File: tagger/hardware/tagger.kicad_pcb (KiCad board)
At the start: 4 copper layers, 70 x 40 mm, 77 parts, among them J1 XBEE_BOOTLOADER, J2 MICRO_SD_CARD, J4 SWD, J6 TETHER_POWER, J7 TETHER_DATA, J8 DISPLAY, J9 IO_CONN, SW1 COMMISSION, SW2 RESET, SW24 BOOT0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

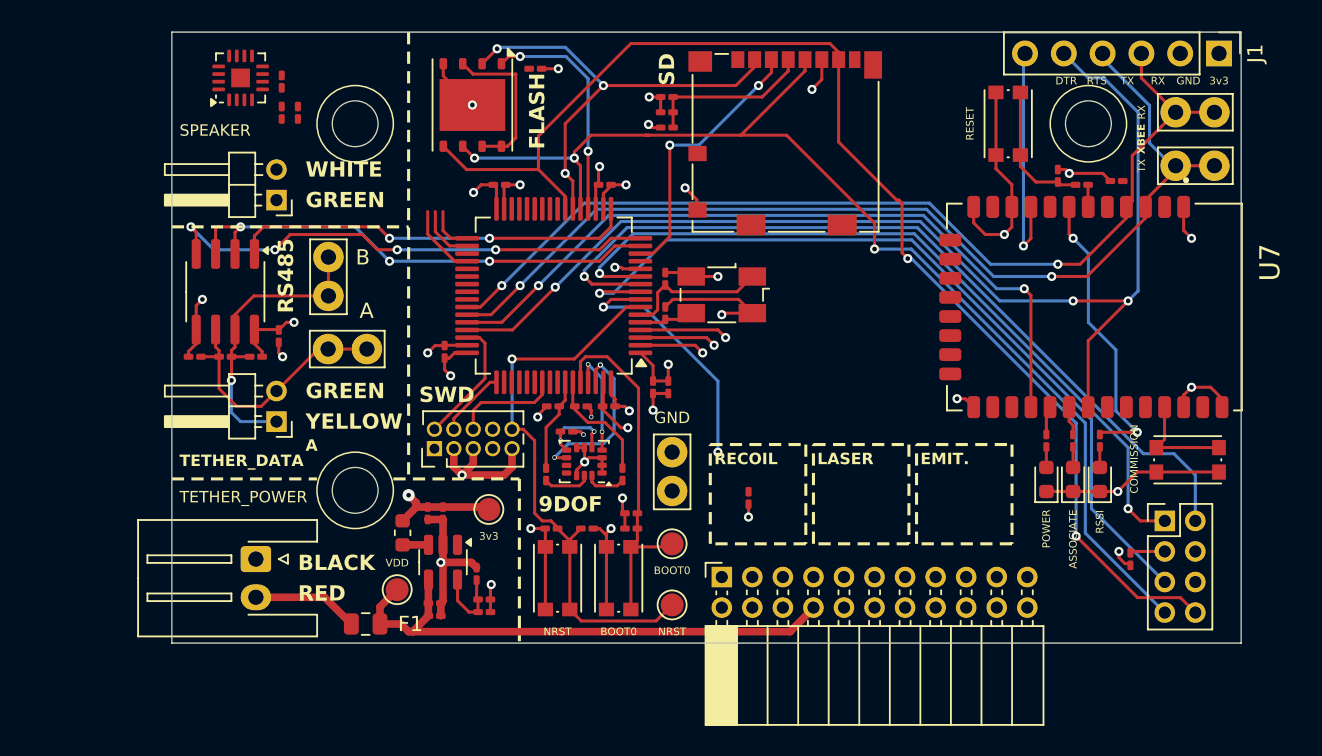
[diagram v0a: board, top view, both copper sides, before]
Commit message: feat: add IR routing, fix component sizes
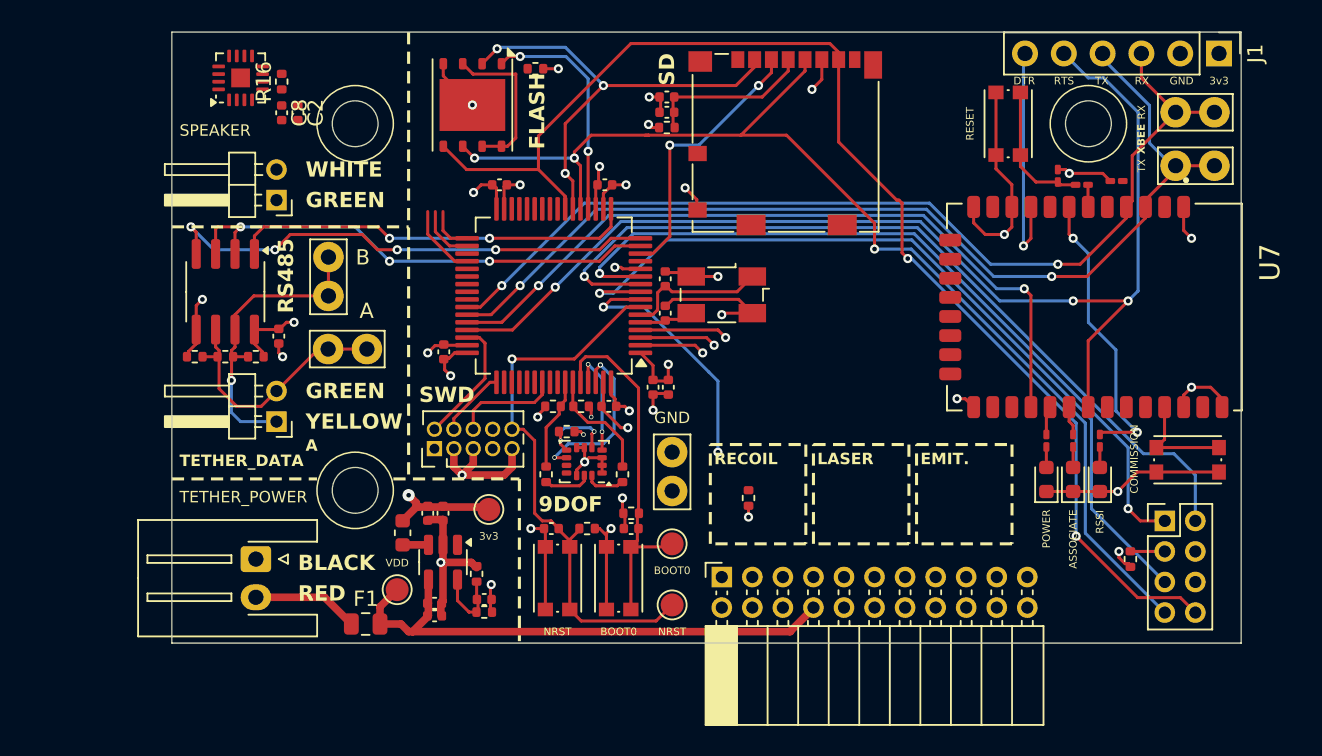
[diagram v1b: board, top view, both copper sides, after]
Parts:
- C1, C10, C100, C101, C102, C103, C104, C2, C3, C4, C5, C6, C63, C64, C66, C68, C7, C8, C9, C99: footprint Capacitor_SMD:C_0201_0603Metric_Pad0.64x0.40mm_HandSolder -> Capacitor_SMD:C_0402_1005Metric
- R10, R11, R13, R16, R17, R18, R19, R2, R20, R21, R25, R26, R5, R6, R7, R8, R9: footprint Resistor_SMD:R_0201_0603Metric_Pad0.64x0.40mm_HandSolder -> Resistor_SMD:R_0402_1005Metric
- moved C102 0.06 mm to (133.8, 97.9)
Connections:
- J9 pad 4: /IR_EMITTER+ -> +3.3V
- U2 pad 29: unconnected-(U2-PB10-Pad29) -> /IrDA_TX
- U2 pad 30: unconnected-(U2-PB11-Pad30) -> /IrDA_RX

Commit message: feat: added missing 3d models
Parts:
- J7, LS3: footprint Connector_PinHeader_2.00mm:PinHeader_1x02_P2.00mm_Horizontal -> tagger:S02B-PASK-2
- moved LS3 3.05 mm to (121.9, 85.1), turned to 90 degrees
- moved J7 1.45 mm to (121.9, 101.4), turned to 90 degrees
- moved SW2 0.90 mm to (170.8, 83.9)
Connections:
- R19 pad 2: Net-(J7-Pin_1) -> Net-(J7-Pin_2)
- R20 pad 1: Net-(J7-Pin_2) -> Net-(J7-Pin_1)
- R21 pad 1: Net-(J7-Pin_1) -> Net-(J7-Pin_2)
- R21 pad 2: Net-(J7-Pin_2) -> Net-(J7-Pin_1)
- TP1 pad 1: Net-(J7-Pin_1) -> Net-(J7-Pin_2)
- TP2 pad 1: Net-(J7-Pin_2) -> Net-(J7-Pin_1)
- U4 pad 6: Net-(J7-Pin_2) -> Net-(J7-Pin_1)
- U4 pad 7: Net-(J7-Pin_1) -> Net-(J7-Pin_2)
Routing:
- net Net-(J7-Pin_2): track 16.9 -> 19.8 mm, vias 0 -> 1
- net Net-(J7-Pin_1): track 20.0 -> 17.2 mm, vias 1 -> 0
- net +3.3V: track 45.6 -> 48.4 mm
- net GND: track 107.7 -> 106.8 mm
- net Net-(R15-Pad1): track 8.96 -> 8.21 mm

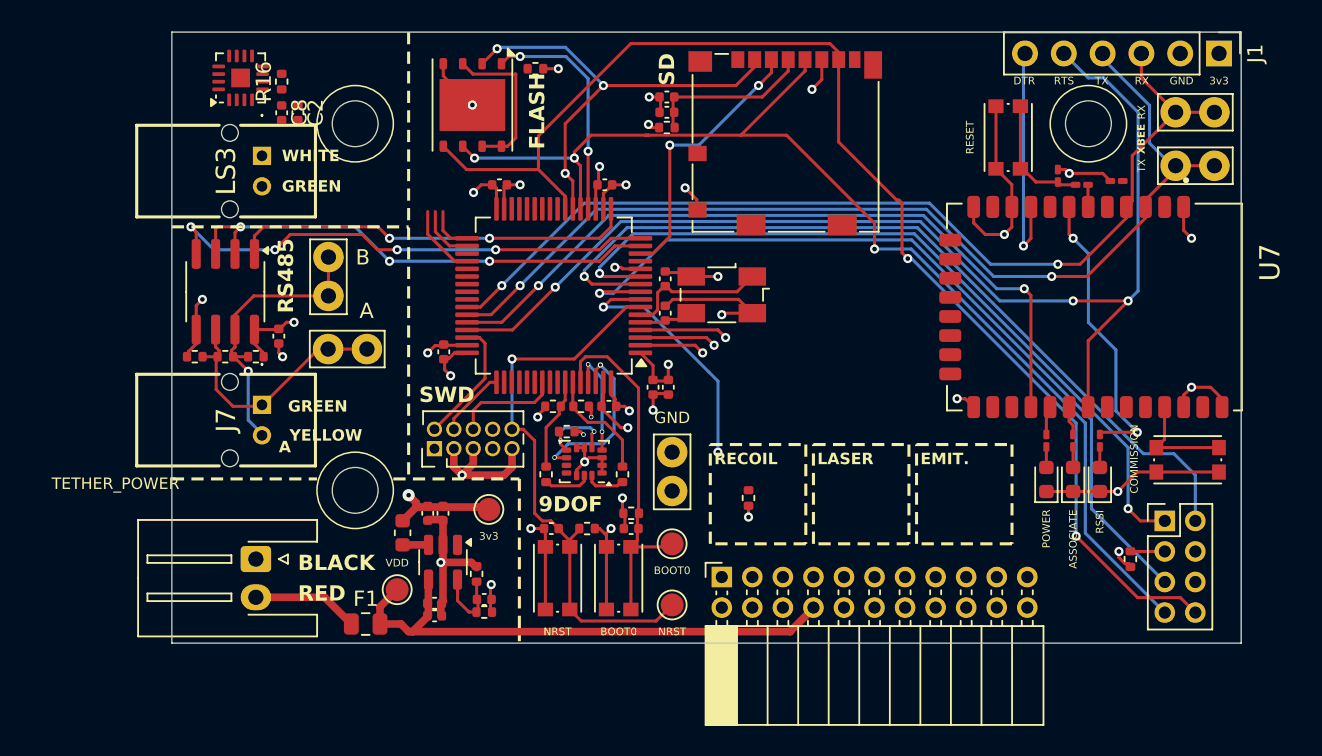
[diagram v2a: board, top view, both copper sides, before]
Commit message: feat: audio routing and test points
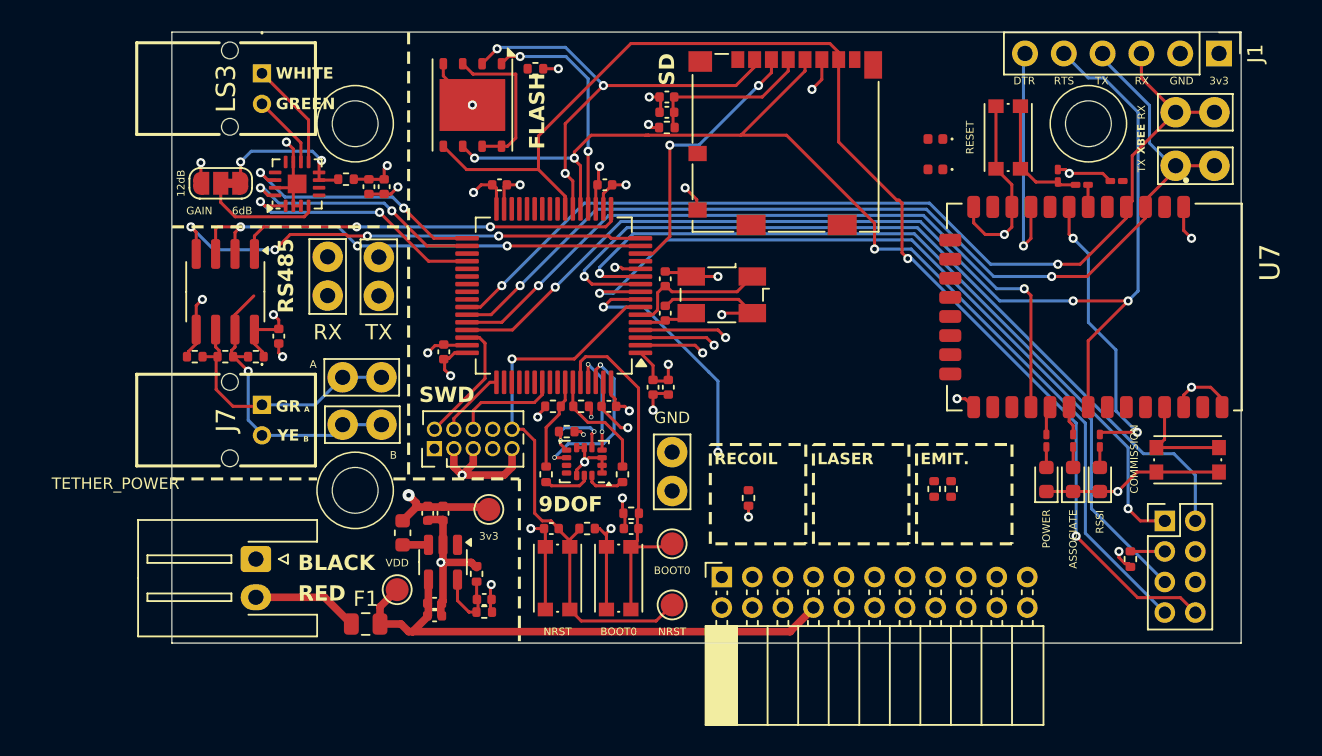
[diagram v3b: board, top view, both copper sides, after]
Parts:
- added D8: D, Diode_SMD:D_0402_1005Metric, F.Cu at (166.0, 86.0)
- added D9: D, Diode_SMD:D_0402_1005Metric, F.Cu at (166.0, 84.0)
- added JP2: GAIN, Jumper:SolderJumper-3_P1.3mm_Bridged12_RoundedPad1.0x1.5mm_NumberLabels, F.Cu at (119.2, 86.9)
- added R12: R, Resistor_SMD:R_0402_1005Metric, F.Cu at (165.9, 106.9)
- added R23: 0R, Resistor_SMD:R_0402_1005Metric, F.Cu at (167.0, 106.9)
- added TP8: RX, TestPoint:TestPoint_Bridge_Pitch2.54mm_Drill1.0mm, F.Cu at (126.2, 94.2)
- added TP9: TX, TestPoint:TestPoint_Bridge_Pitch2.54mm_Drill1.0mm, F.Cu at (129.6, 94.3)
- moved TP1 9.12 mm to (129.7, 102.7), turned to 180 degrees
- moved U8 7.86 mm to (124.2, 86.9)
- moved R16 7.65 mm to (127.4, 86.6), turned to 180 degrees
- moved C8 7.48 mm to (128.9, 87.1)
- moved C2 7.44 mm to (129.9, 87.1)
- moved LS3 5.40 mm to (121.9, 79.7)
- moved TP2 2.08 mm to (127.2, 99.6)
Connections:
- R16 pad 2: Net-(U8-~{SD_MODE}) -> Net-(JP2-A)
- U8 pad 4: Net-(U8-~{SD_MODE}) -> Net-(JP2-C)
- U8 pad 7: Net-(U8-~{SD_MODE}) -> Net-(JP2-A)
- U8 pad 8: Net-(U8-~{SD_MODE}) -> Net-(JP2-A)
- U9 pad 2: /SPI_POCI -> /SPI_PICO
- U9 pad 5: /SPI_PICO -> /SPI_POCI
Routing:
- net /DAC_LRCLK: track 3.03 -> 16.5 mm, vias 0 -> 2
- net /DAC_BCLK: track 3.78 -> 16.3 mm, vias 0 -> 2
- net /DAC_DIN: track 4.79 -> 16.9 mm, vias 0 -> 2
- net Net-(JP2-A): track 0.00 -> 9.87 mm, vias 0 -> 2
- net GND: track 106.8 -> 116.5 mm, vias 25 -> 28
- net Net-(JP2-C): track 0.00 -> 7.64 mm
- net Net-(U8-OUTP): track 0.00 -> 7.07 mm
- net Net-(U8-OUTN): track 0.00 -> 4.86 mm
- net +3.3V: track 48.4 -> 51.3 mm, vias 16 -> 17
- net /TETHER_RTS: track 32.8 -> 31.9 mm
- net /TETHER_RX: track 26.6 -> 25.7 mm
- net Net-(J7-Pin_2): track 19.8 -> 20.5 mm
- net /TETHER_TX: track 33.1 -> 32.5 mm
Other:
- board text added: "B"
- board text added: "GR"
- board text added: "REV 2: - Rotate stm32 90deg - put XBee where stm32 and flash are - shift SD card to right OR swap stm32 to SD card position move RF module to stm32 position mode SD card to RF module position"
- board text added: "YE"
- board text removed: "REV 2: - Rotate stm32 90deg - put XBee stm32 and flash are - shift SD card to right OR swap stm32 to SD card position move RF module to stm32 position mode SD card to RF module position"
- board text removed: "YELLOW"

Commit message: feat: more pcb layout
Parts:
- moved R12 13.8 mm to (152.2, 106.9)
- moved R23 13.8 mm to (153.3, 106.9)
- moved R5 5.17 mm to (158.8, 106.6)
- moved C101 1.54 mm to (136.2, 87.9), turned to 90 degrees
- moved TP8 1.03 mm to (126.3, 93.2), turned to -90 degrees
- moved TP9 1.03 mm to (129.7, 93.2), turned to -90 degrees
- moved TP6 0.15 mm to (148.6, 114.5)
- moved TP7 0.15 mm to (148.6, 110.5)
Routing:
- net /GRIP_DOUT: track 0.00 -> 37.6 mm, vias 0 -> 1
- net /BTN_RELOAD: track 5.78 -> 35.1 mm, vias 1 -> 0
- net /BTN_TRIGGER: track 4.28 -> 33.5 mm
- net /BTN_MENU: track 5.03 -> 32.7 mm, vias 1 -> 0
- net /IrDA_RX: track 0.00 -> 27.4 mm, vias 0 -> 2
- net /IrDA_TX: track 0.00 -> 25.4 mm, vias 0 -> 2
- net /FRONT_IR: track 0.00 -> 9.41 mm
- net /TETHER_RX: track 25.7 -> 33.9 mm
- net /MOTOR: track 16.8 -> 24.7 mm
- net /IR_EMITTER-: track 0.00 -> 6.02 mm
- net /TETHER_TX: track 32.5 -> 38.2 mm
- net /DISPLAY_D/C: track 55.2 -> 51.6 mm
- net /SPI_PICO: track 83.0 -> 86.4 mm
- net /DISPLAY_RST: track 51.2 -> 48.0 mm
- net GND: track 116.5 -> 117.6 mm, vias 28 -> 27
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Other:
- board text added: "WH"
- board text removed: "GREEN"
- board text removed: "WHITE"

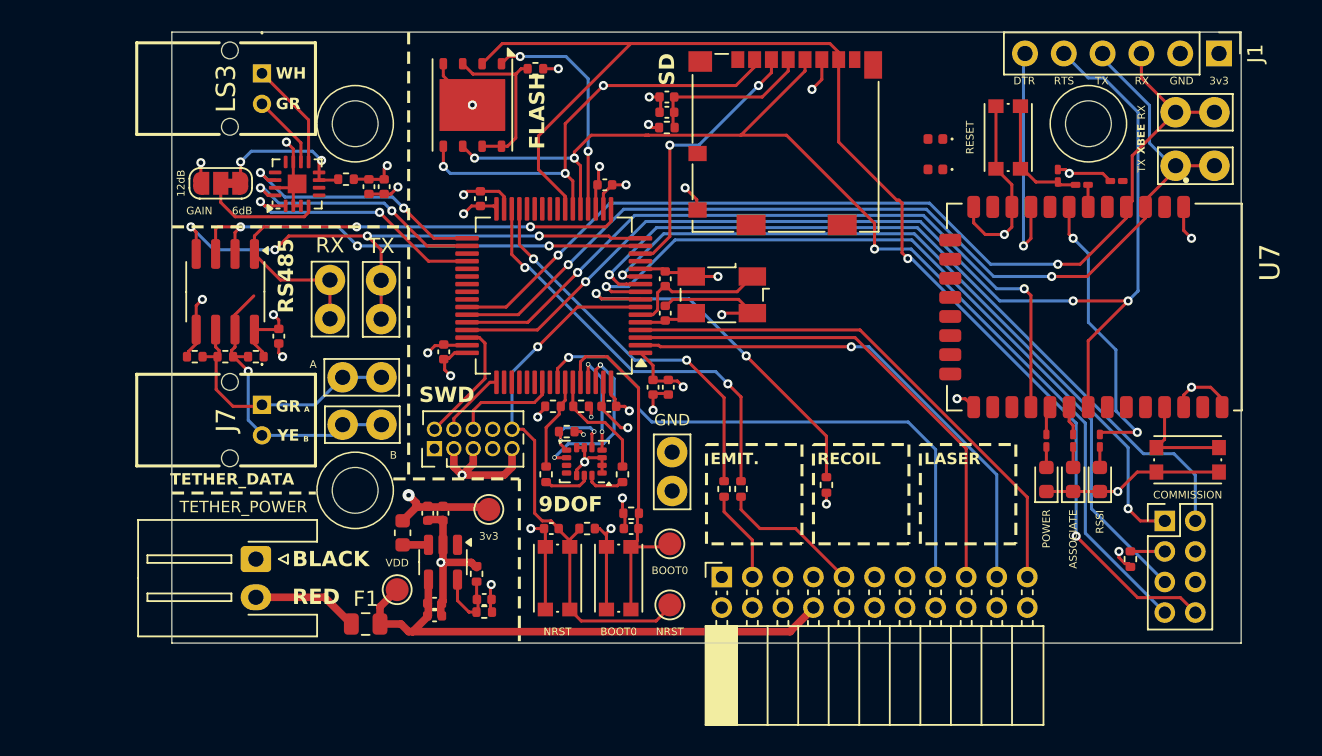
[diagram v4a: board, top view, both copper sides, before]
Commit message: feat: replace RS485 transceiver, fix DRC warnings
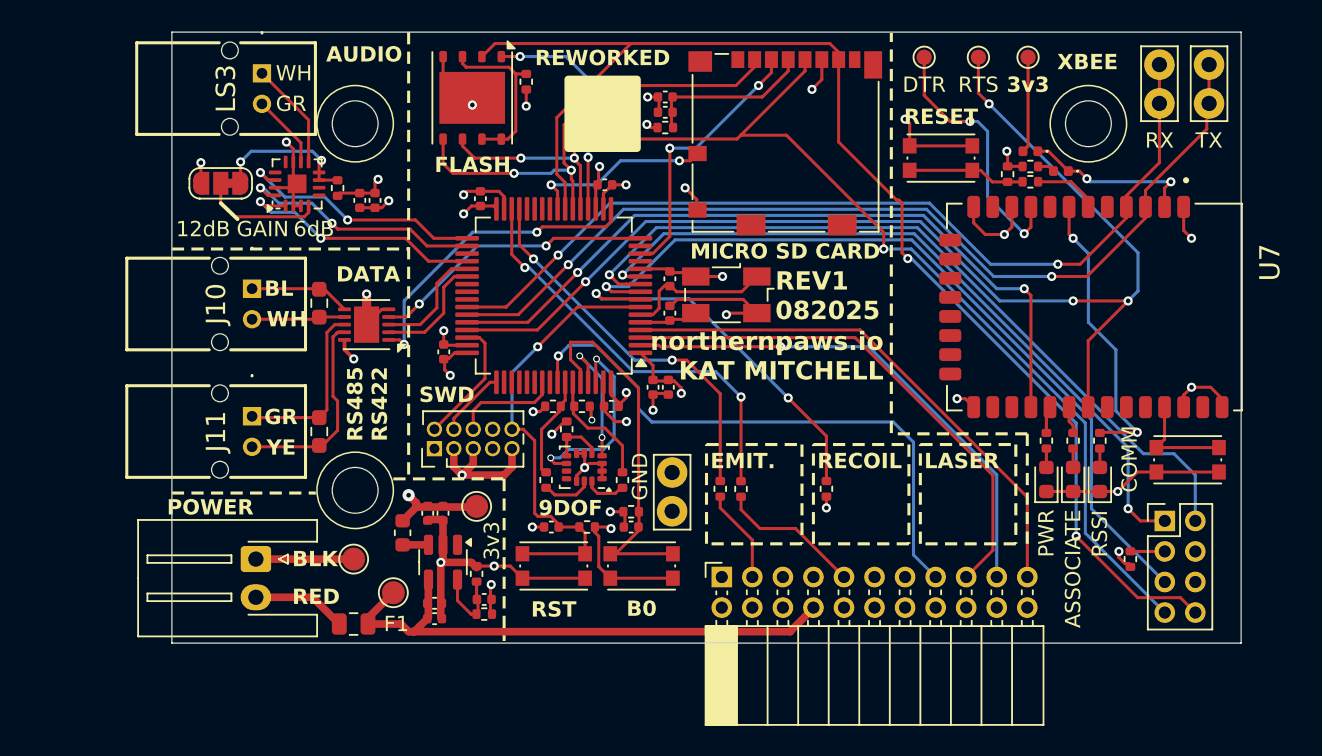
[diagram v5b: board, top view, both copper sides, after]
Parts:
- removed C104: 100nF, Capacitor_SMD:C_0402_1005Metric
- removed J1: XBEE_BOOTLOADER, Connector_PinHeader_2.54mm:PinHeader_1x06_P2.54mm_Vertical
- removed J7: TETHER_DATA, tagger:S02B-PASK-2
- removed R19, R20: 500R, Resistor_SMD:R_0402_1005Metric
- removed R21: 130R, Resistor_SMD:R_0402_1005Metric
- removed TP1: B, TestPoint:TestPoint_Bridge_Pitch2.54mm_Drill1.0mm
- removed TP2: A, TestPoint:TestPoint_Bridge_Pitch2.54mm_Drill1.0mm
- removed TP6: NRST, TestPoint:TestPoint_Pad_D1.5mm
- removed TP7: BOOT0, TestPoint:TestPoint_Pad_D1.5mm
- removed U4: ST3485EB, Package_SO:SOIC-8_3.9x4.9mm_P1.27mm
- added J10: TETHER_TX, tagger:S02B-PASK-2, F.Cu at (121.2, 93.8)
- added J11: TETHER_RX, tagger:S02B-PASK-2, F.Cu at (121.2, 102.2)
- added R22: 120R, Resistor_SMD:R_0603_1608Metric_Pad0.98x0.95mm_HandSolder, F.Cu at (125.7, 103.2)
- added R24: 120R, Resistor_SMD:R_0603_1608Metric_Pad0.98x0.95mm_HandSolder, F.Cu at (125.7, 94.8)
- added TP10: DTR, TestPoint:TestPoint_Pad_D1.0mm, F.Cu at (165.2, 78.7)
- added TP17: GND, TestPoint:TestPoint_Pad_D1.5mm, F.Cu at (127.9, 111.5)
- added U3: LTC2852xDD, Package_DFN_QFN:DFN-10-1EP_3x3mm_P0.5mm_EP1.65x2.38mm, F.Cu at (128.8, 96.2)
- D6: value POWER -> PWR
- J6: value TETHER_POWER -> POWER
- R1, R14, R15, R27, R3, R4: footprint Resistor_SMD:R_0201_0603Metric_Pad0.64x0.40mm_HandSolder -> Resistor_SMD:R_0402_1005Metric
- R18: value 20.0 k -> 20.0k
- SW1: value COMMISSION -> COMM
- SW24: value BOOT0 -> B0
- SW26: value NRST -> RST
- TP8: value RX -> 3v3; footprint TestPoint:TestPoint_Bridge_Pitch2.54mm_Drill1.0mm -> TestPoint:TestPoint_Pad_D1.0mm
- TP9: value TX -> RTS; footprint TestPoint:TestPoint_Bridge_Pitch2.54mm_Drill1.0mm -> TestPoint:TestPoint_Pad_D1.0mm
- moved TP8 48.0 mm to (172.1, 78.7), turned to 0 degrees
- moved TP9 41.7 mm to (168.8, 78.7), turned to 0 degrees
- moved D8 8.22 mm to (174.2, 86.1)
- moved TP3 6.63 mm to (183.9, 79.1), turned to -90 degrees
- moved D9 6.27 mm to (172.2, 84.8)
- moved R14 5.72 mm to (172.2, 85.8)
- moved TP4 4.76 mm to (180.7, 79.1), turned to -90 degrees
- moved SW2 4.60 mm to (166.3, 85.2), turned to 0 degrees
- moved R15 3.37 mm to (172.2, 86.8)
- moved R27 3.29 mm to (170.7, 86.3)
- moved SW24 1.70 mm to (146.8, 112.0), turned to 180 degrees
- moved TP5 1.33 mm to (148.8, 108.4)
- moved C2 1.08 mm to (129.3, 88.0)
- moved C8 1.08 mm to (128.3, 88.0)
- moved R10 1.04 mm to (139.2, 80.2), turned to 90 degrees
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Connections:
- D9 pad 2: /RF/UART_PWR -> Net-(D9-A)
- J2 pad 9: /Peripherals/SD_DETECT -> /SD_DETECT
- TP8 pad 1: /TETHER_RX -> Net-(D9-A)
- TP9 pad 1: /TETHER_TX -> /RF/RF_UART_RTS
- U2 pad 15: /TETHER_RTS -> unconnected-(U2-PA1-Pad15)
- U2 pad 24: unconnected-(U2-PC4-Pad24) -> /SD_DETECT
- U2 pad 37: unconnected-(U2-PC6-Pad37) -> /TETHER_DRIV_EN
- U2 pad 38: unconnected-(U2-PC7-Pad38) -> /TETHER_RECV_EN
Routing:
- net /TETHER_RTS: track 31.9 -> 0.00 mm, vias 3 -> 0
- net Net-(J7-Pin_2): track 20.5 -> 0.00 mm, vias 1 -> 0
- net /TETHER_TX: track 38.2 -> 18.6 mm, vias 4 -> 2
- net Net-(J7-Pin_1): track 17.3 -> 0.00 mm
- net /TETHER_RX: track 33.9 -> 20.5 mm
- net Net-(J11-Pin_2): track 0.00 -> 13.2 mm
- net /SD_DETECT: track 0.00 -> 12.2 mm, vias 0 -> 2
- net Net-(J11-Pin_1): track 0.00 -> 11.6 mm
- net Net-(D8-K): track 0.00 -> 11.4 mm, vias 0 -> 2
- net /TETHER_RECV_EN: track 0.00 -> 7.63 mm
- net /TETHER_DRIV_EN: track 0.00 -> 7.57 mm
- net /SWD_RESET: track 37.0 -> 29.9 mm
- net Net-(J10-Pin_1): track 0.00 -> 6.61 mm
- net Net-(D9-A): track 0.00 -> 6.29 mm
- net Net-(J10-Pin_2): track 0.00 -> 6.11 mm
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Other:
- board text added: "AUDIO"
- board text added: "BL"
- board text added: "BLK"
- board text added: "DATA"
- board text added: "MICRO SD CARD"
- board text added: "REV1 082025"
- board text added: "REWORKED"
- board text added: "RS485 RS422"
- board text added: "northernpaws.io KAT MITCHELL"
- board text removed: "3v3"
- board text removed: "A"
- board text removed: "B"
- board text removed: "BLACK"
- board text removed: "DTR"
- board text removed: "GND"
- board text removed: "RS485"
- board text removed: "RTS"
- board text removed: "RX"
- board text removed: "SD"
- board text removed: "TX"
